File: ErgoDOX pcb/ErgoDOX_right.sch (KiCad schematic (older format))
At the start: 105 parts, among them J1 AudioJack4, J2 USB_B_Micro, SW0:10 SW0:3, SW0:11 SW0:2, SW0:12 SW0:1, SW0:7 SW0:6, SW0:8 SW0:5, SW0:9 SW0:4, SW1 TS-1187A-B-A-B, SW1:10 SW1:3, SW1:11 SW1:2, SW1:12 SW1:1, SW1:13 SW1:0, SW1:9 SW1:4, SW2:10 SW2:3, SW2:11 SW2:2, SW2:12 SW2:1, SW2:13 SW2:0, SW2:7 SW2:6, SW2:8 SW2:5, SW2:9 SW2:4, SW3:10 SW3:3, SW3:11 SW3:2, SW3:12 SW3:1, SW3:13 SW3:0, SW3:8 SW3:5, SW3:9 SW3:4, SW4:10 SW4:3, SW4:11 SW4:2, SW4:12 SW4:1, SW4:13 SW4:0, SW4:7 SW4:6, SW4:8 SW4:5, SW4:9 SW4:4, SW5:10 SW5:3, SW5:11 SW5:2, SW5:12 SW5:1, SW5:13 SW5:0, SW5:7 SW5:6, SW5:8 SW5:5, SW5:9 SW5:4, U1 ATmega32U4-MU, U2 MCP23018, Y1 16MHz

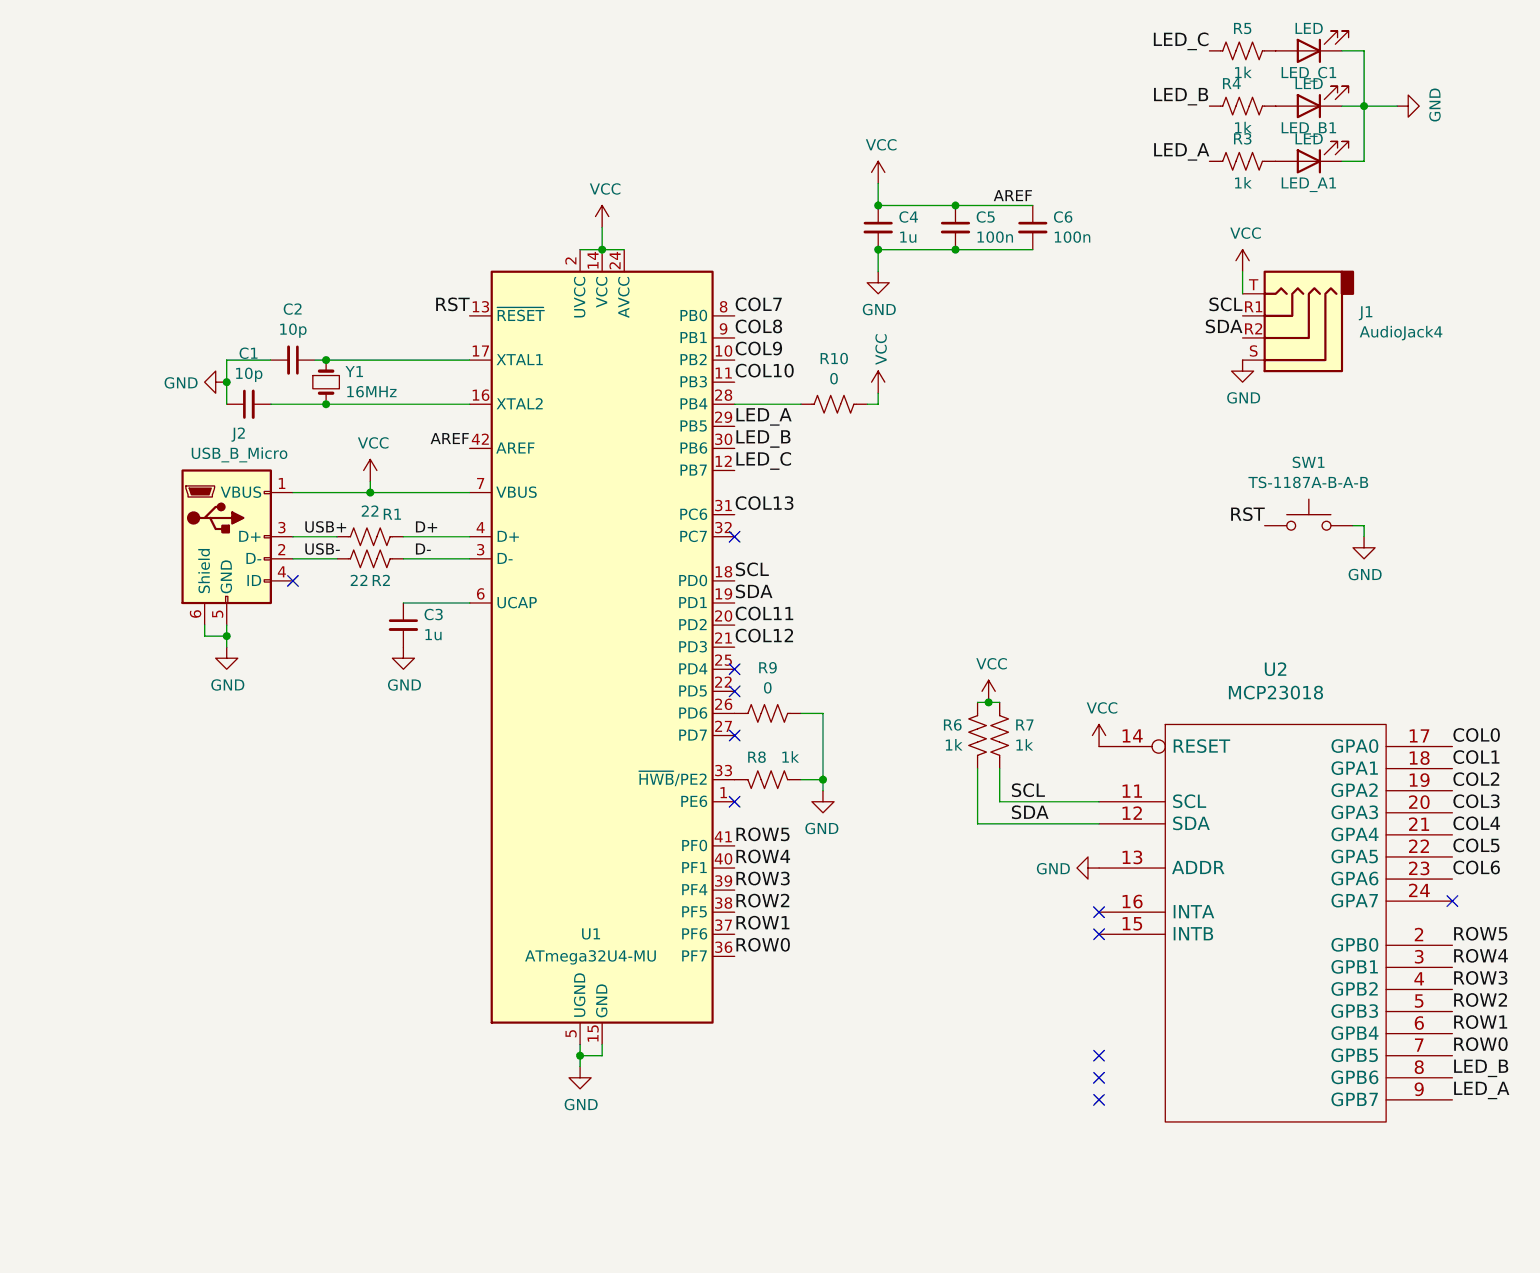
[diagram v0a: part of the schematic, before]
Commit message: Routed RH board
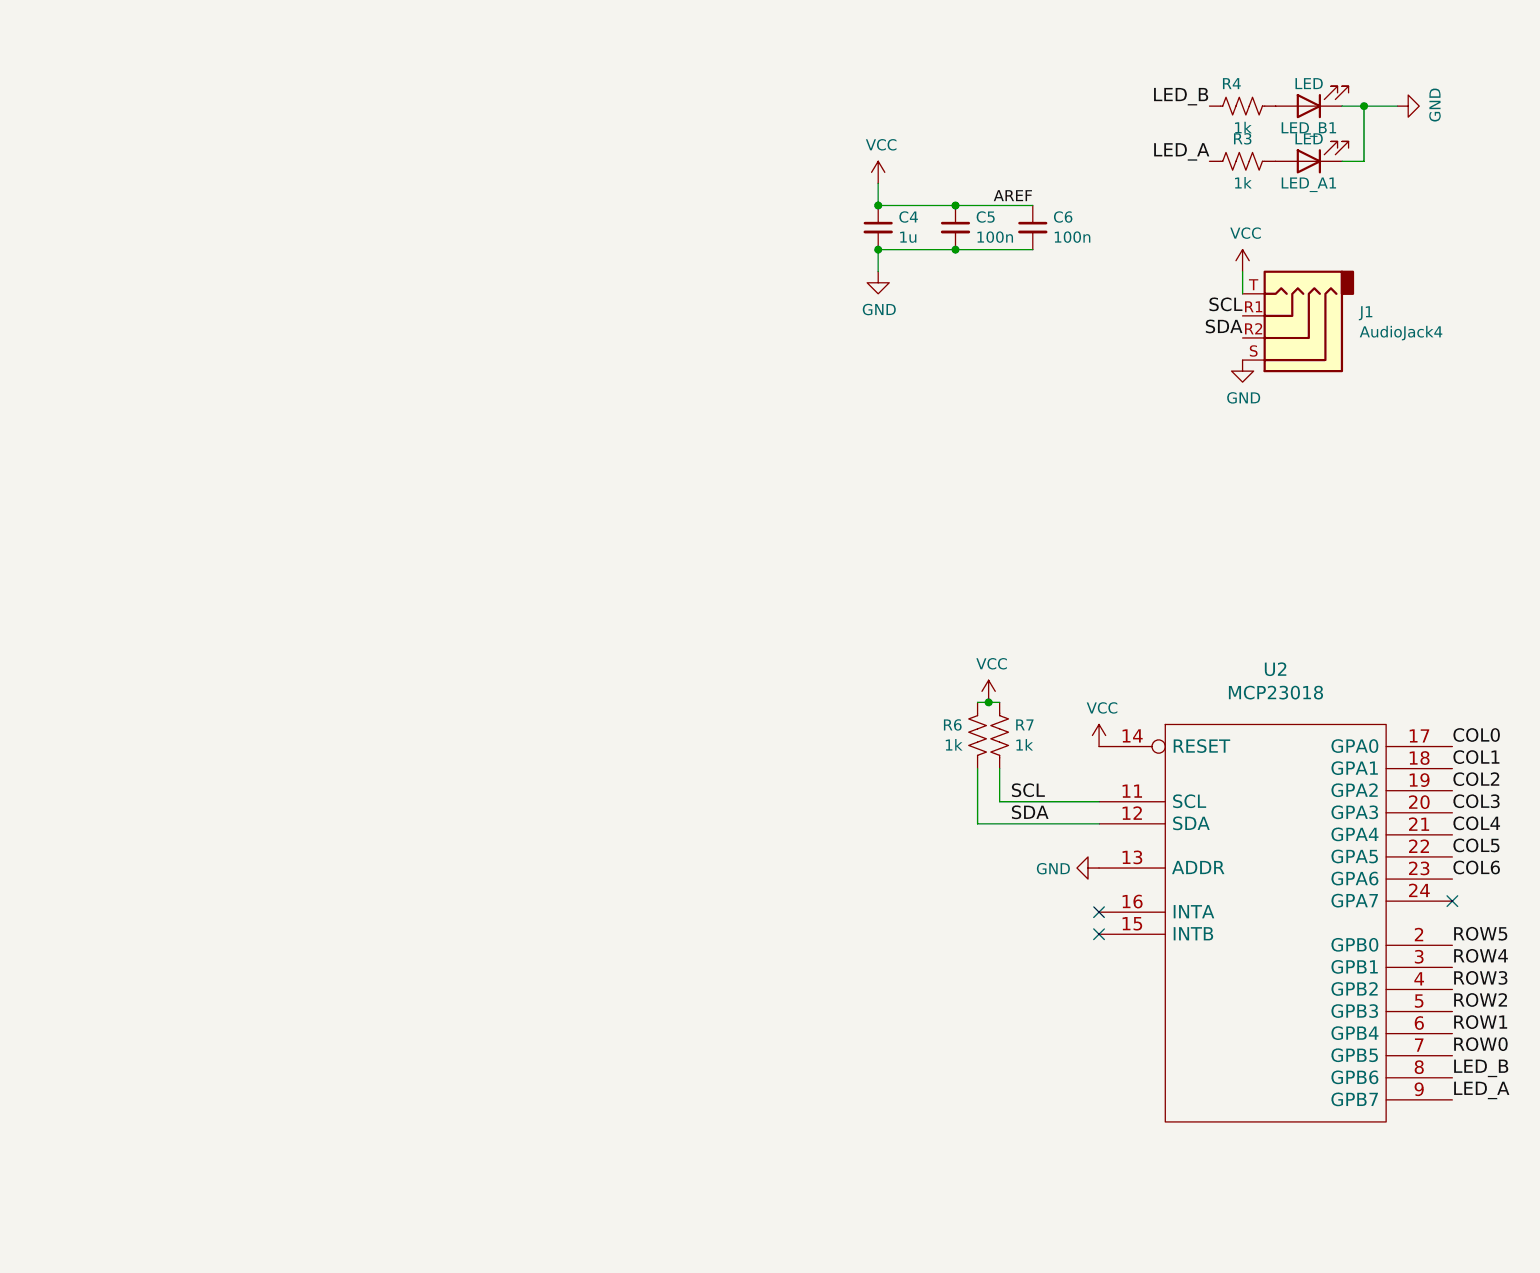
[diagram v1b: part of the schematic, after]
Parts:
- removed C1, C2: 10p, Capacitors_SMD:C_0603, symbol Device:C_Small
- removed C3: 1u, Capacitors_SMD:C_0603, symbol Device:C_Small
- removed J2: USB_B_Micro, Connectors_USB:USB_Micro-B_Wuerth-629105150521, symbol Connector:USB_B_Micro
- removed LED_C1: LED, LEDs:LED_0603, symbol Device:LED
- removed R1, R2: 22, Resistors_SMD:R_0603, symbol Device:R_US
- removed R10, R9: 0, Resistors_SMD:R_0603, symbol Device:R_US
- removed R5, R8: 1k, Resistors_SMD:R_0603, symbol Device:R_US
- removed SW1: TS-1187A-B-A-B, Buttons_Switches_THT:SW_PUSH_6mm, symbol Switch:SW_Push
- removed U1: ATmega32U4-MU, Housings_DFN_QFN:QFN-44-1EP_7x7mm_Pitch0.5mm, symbol MCU_Microchip_ATmega:ATmega32U4-MU
- removed Y1: 16MHz, Crystals:Crystal_SMD_3225-4pin_3.2x2.5mm, symbol Device:Crystal_Small
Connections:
- no-connect marks 12 -> 3

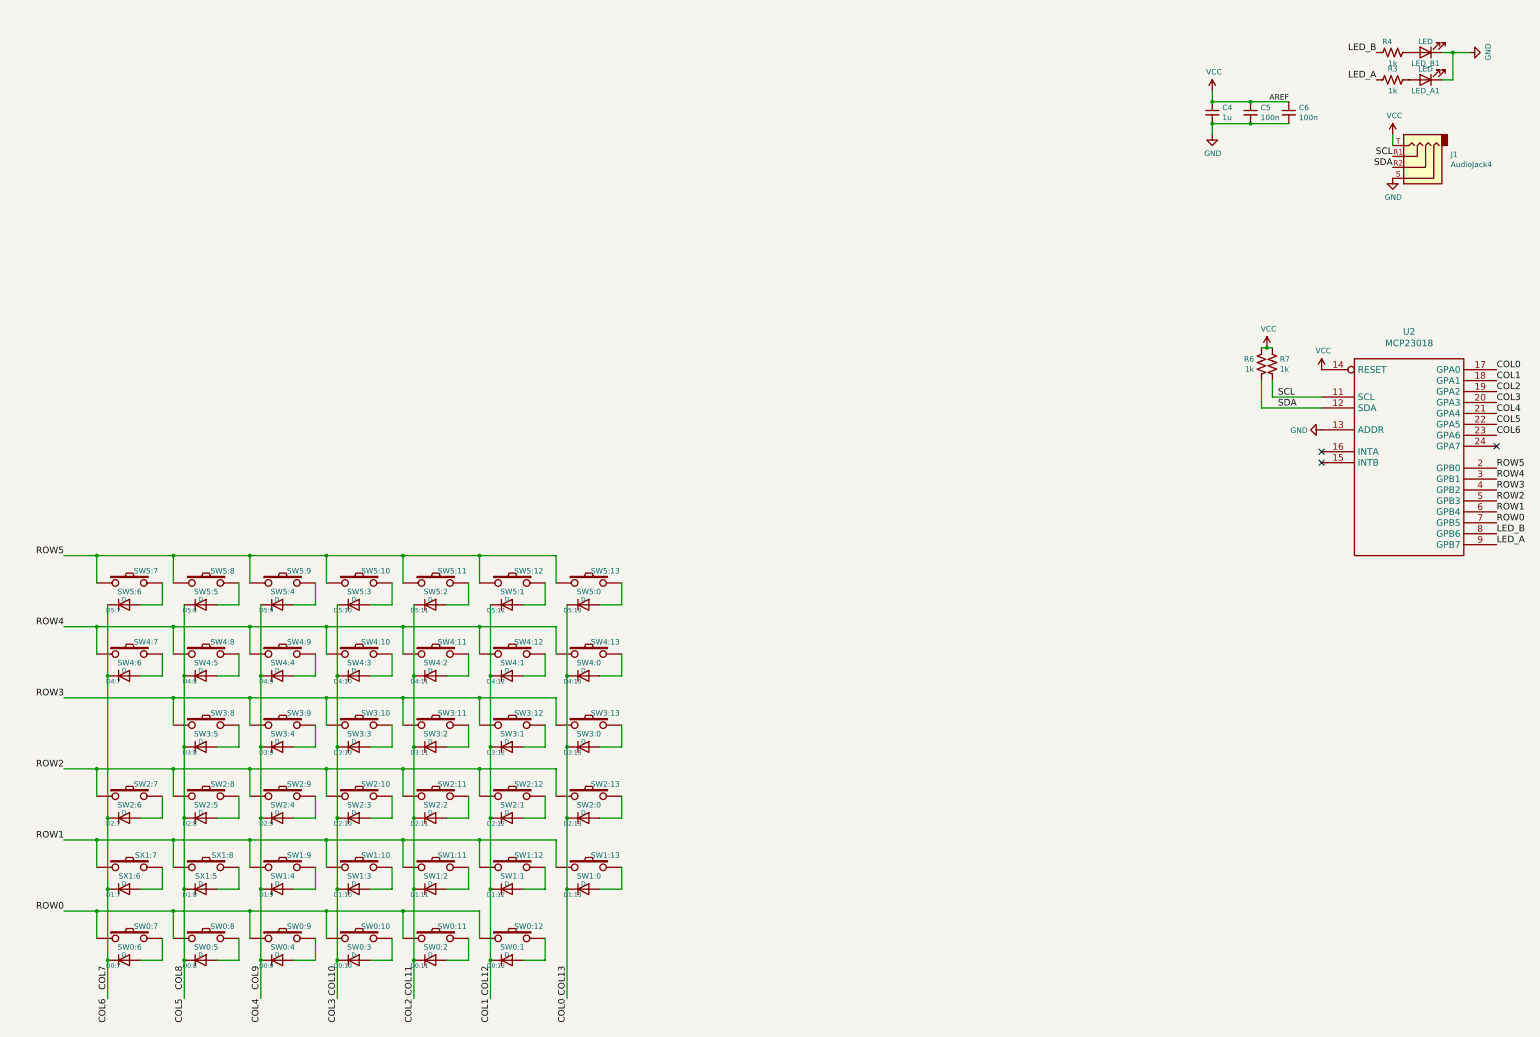
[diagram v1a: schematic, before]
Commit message: Added revision, generated gerbers
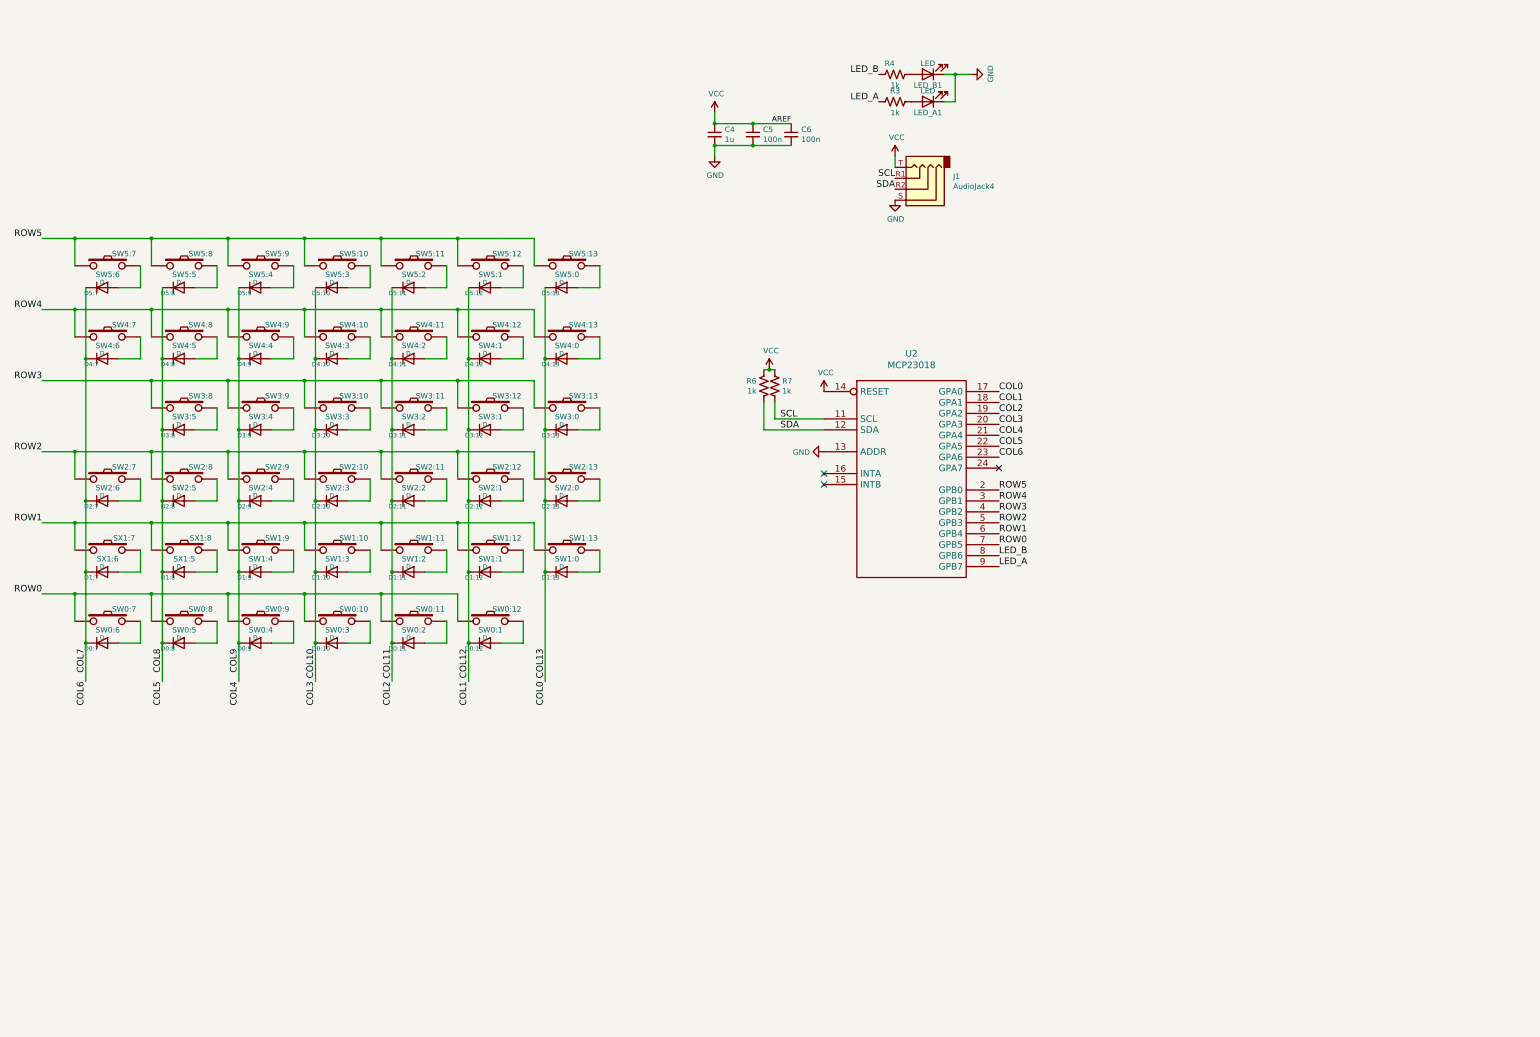
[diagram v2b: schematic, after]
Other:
- moved on the sheet: C4, C5, C6, D0:10, D0:11, D0:12, D0:7, D0:8, D0:9, D1:10, D1:11, D1:12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

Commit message: Switched MCP23018 to SOIC package
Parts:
- U2: footprint Housings_SSOP:SSOP-24_5.3x8.2mm_Pitch0.65mm -> Housings_SOIC:SOIC-28W_7.5x17.9mm_Pitch1.27mm; symbol ErgoDOX:MCP23018 -> ErgoDOX:MCP23018_SOIC
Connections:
- net COL0: now also U2.20 (GPA0); no longer U2.17 (GPA0)
- net COL1: now also U2.21 (GPA1); no longer U2.18 (GPA1)
- net COL10: now also U2.23 (GPA3); no longer U2.20 (GPA3)
- net COL11: now also U2.22 (GPA2); no longer U2.19 (GPA2)
- net COL4: now also U2.24 (GPA4); no longer U2.21 (GPA4)
- net COL5: now also U2.25 (GPA5); no longer U2.22 (GPA5)
- net COL6: now also U2.26 (GPA6); no longer U2.23 (GPA6)
- net GND: now also U2.15 (ADDR); no longer U2.13 (ADDR)
- net LED_A: now also U2.10 (GPB7); no longer U2.9 (GPB7)
- net LED_B: now also U2.9 (GPB6); no longer U2.8 (GPB6)
- net ROW0: now also U2.8 (GPB5); no longer U2.7 (GPB5)
- net ROW1: now also U2.7 (GPB4); no longer U2.6 (GPB4)
- net ROW2: now also U2.6 (GPB3); no longer U2.5 (GPB3)
- net ROW3: now also U2.5 (GPB2); no longer U2.4 (GPB2)
- net ROW4: now also U2.4 (GPB1); no longer U2.3 (GPB1)
- net ROW5: now also U2.3 (GPB0); no longer U2.2 (GPB0)
- net SCL: now also U2.12 (SCL); no longer U2.11 (SCL)
- net SDA: now also U2.13 (SDA); no longer U2.12 (SDA)
- net VCC: now also U2.11 (VCC), U2.16 (RESET); no longer U2.10 (VCC), U2.14 (RESET)
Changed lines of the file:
@@
 Sheet 1 1
 Title "ErgoDox Right"
-Date "2020-10-12"
-Rev "2.0.0"
+Date "2020-11-01"
+Rev "2.0.1"
 Comp "Offline Systems LLC"
 Comment1 ""
@@
 $EndComp
 $Comp
-L ErgoDOX:MCP23018 U2
+L ErgoDOX:MCP23018_SOIC U2
 U 1 1 5F78DF8E
 P 9050 5100
 F 0 "U2" H 9050 6248 60  0000 C CNN
 F 1 "MCP23018" H 9050 6142 60  0000 C CNN
-F 2 "Housings_SSOP:SSOP-24_5.3x8.2mm_Pitch0.65mm" H 9050 5100 50  0001 C CNN
+F 2 "Housings_SOIC:SOIC-28W_7.5x17.9mm_Pitch1.27mm" H 9050 5100 50  0001 C CNN
 F 3 "" H 9050 5100 50  0001 C CNN
 	1    9050 5100
